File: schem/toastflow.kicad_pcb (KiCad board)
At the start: 2 copper layers, 40 x 25 mm, 23 parts, among them IC1 ATTINY13, K1 CONN_3, P1 CONN_3X2, SW1 SW_PUSH, U1 TRIAC

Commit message: Blank code
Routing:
- net VCC: track 54.1 -> 55.0 mm, vias 2 -> 1
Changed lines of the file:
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@@
     (links 38)
     (no_connects 0)
-    (area 0 0 0 0)
+    (area 32.924999 36.424999 75.486111 63.5196)
     (thickness 1.6)
     (drawings 8)
-    (tracks 107)
+    (tracks 102)
     (zones 0)
     (modules 23)
@@
       (viasonmask false)
       (mode 1)
-      (useauxorigin false)
+      (useauxorigin true)
       (hpglpennumber 1)
       (hpglpenspeed 20)
@@
     (fp_line (start 11.5 4.5) (end -11.5 4.5) (layer F.SilkS) (width 0.15))
     (fp_line (start -11.5 4.5) (end -11.5 -4.5) (layer F.SilkS) (width 0.15))
-    (pad 1 thru_hole circle (at -7.5 0) (size 1.8 1.8) (drill 1.2)
+    (pad 1 thru_hole circle (at -7.5 0) (size 1.8 1.8) (drill 1.199999)
       (layers *.Cu *.Mask F.SilkS)
       (net 8 N-0000013)
     )
-    (pad 2 thru_hole circle (at 7.5 0) (size 1.8 1.8) (drill 1.2)
+    (pad 2 thru_hole circle (at 7.5 0) (size 1.8 1.8) (drill 1.199999)
       (layers *.Cu *.Mask F.SilkS)
       (net 15 VCC)
@@
     (fp_line (start 5.25 3) (end -5.25 3) (layer F.SilkS) (width 0.15))
     (fp_line (start -5.25 3) (end -5.25 -4) (layer F.SilkS) (width 0.15))
-    (pad 1 thru_hole rect (at -3.5 0 270) (size 2 2) (drill 1.2)
+    (pad 1 thru_hole rect (at -3.5 0 270) (size 2 2) (drill 1.199999)
       (layers *.Cu *.Mask F.SilkS)
       (net 7 N-0000012)
     )
-    (pad 2 thru_hole circle (at 0 0 270) (size 2 2) (drill 1.2)
+    (pad 2 thru_hole circle (at 0 0 270) (size 2 2) (drill 1.199999)
       (layers *.Cu *.Mask F.SilkS)
       (net 13 N-000007)
     )
-    (pad 3 thru_hole circle (at 3.5 0 270) (size 2 2) (drill 1.2)
+    (pad 3 thru_hole circle (at 3.5 0 270) (size 2 2) (drill 1.199999)
       (layers *.Cu *.Mask F.SilkS)
       (net 8 N-0000013)
@@
     (fp_line (start 8.75 2.5) (end -8.75 2.5) (layer F.SilkS) (width 0.15))
     (fp_line (start -8.75 2.5) (end -8.75 -2.5) (layer F.SilkS) (width 0.15))
-    (pad 1 thru_hole circle (at -7.5 0) (size 1 1) (drill 0.6)
+    (pad 1 thru_hole circle (at -7.5 0) (size 1 1) (drill 0.599999)
       (layers *.Cu *.Mask F.SilkS)
       (net 13 N-000007)
     )
-    (pad 2 thru_hole circle (at 7.5 0) (size 1 1) (drill 0.6)
+    (pad 2 thru_hole circle (at 7.5 0) (size 1 1) (drill 0.599999)
       (layers *.Cu *.Mask F.SilkS)
       (net 12 N-000004)
@@
   (segment (start 52.962 41.238) (end 53.2 41.238) (width 0.3) (layer F.Cu) (net 14))
   (segment (start 51.1 43.1) (end 52.962 41.238) (width 0.3) (layer F.Cu) (net 14))
-  (segment (start 55.4 44.2) (end 55.000002 44.599998) (width 0.3) (layer B.Cu) (net 15))
-  (segment (start 58.15 42.75) (end 58.2 42.8) (width 0.3) (layer F.Cu) (net 15))
-  (via (at 58.2 42.8) (size 0.8) (layers F.Cu B.Cu) (net 15))
-  (segment (start 58.2 42.8) (end 56.8 42.8) (width 0.3) (layer B.Cu) (net 15))
-  (segment (start 56.8 42.8) (end 55.4 44.2) (width 0.3) (layer B.Cu) (net 15))
-  (segment (start 57 42.75) (end 58.15 42.75) (width 0.3) (layer F.Cu) (net 15))
-  (segment (start 55.000002 50.870002) (end 58.03 53.9) (width 0.3) (layer B.Cu) (net 15))
-  (segment (start 55.000002 50.300002) (end 55.000002 50.870002) (width 0.3) (layer B.Cu) (net 15))
-  (segment (start 55.000002 44.599998) (end 55.000002 50.300002) (width 0.3) (layer B.Cu) (net 15))
+  (segment (start 58.03 53.9) (end 55.000002 50.870002) (width 0.3) (layer B.Cu) (net 15) (status 400000))
+  (segment (start 57.7 41.8) (end 59.8 41.8) (width 0.3) (layer B.Cu) (net 15) (status 800000))
+  (segment (start 55.000002 44.499998) (end 57.7 41.8) (width 0.3) (layer B.Cu) (net 15))
+  (segment (start 55.000002 50.870002) (end 55.000002 44.499998) (width 0.3) (layer B.Cu) (net 15))
   (segment (start 58.03 53.9) (end 59.33 55.2) (width 0.3) (layer B.Cu) (net 15))
   (segment (start 59.33 55.2) (end 66.1 55.2) (width 0.3) (layer B.Cu) (net 15))

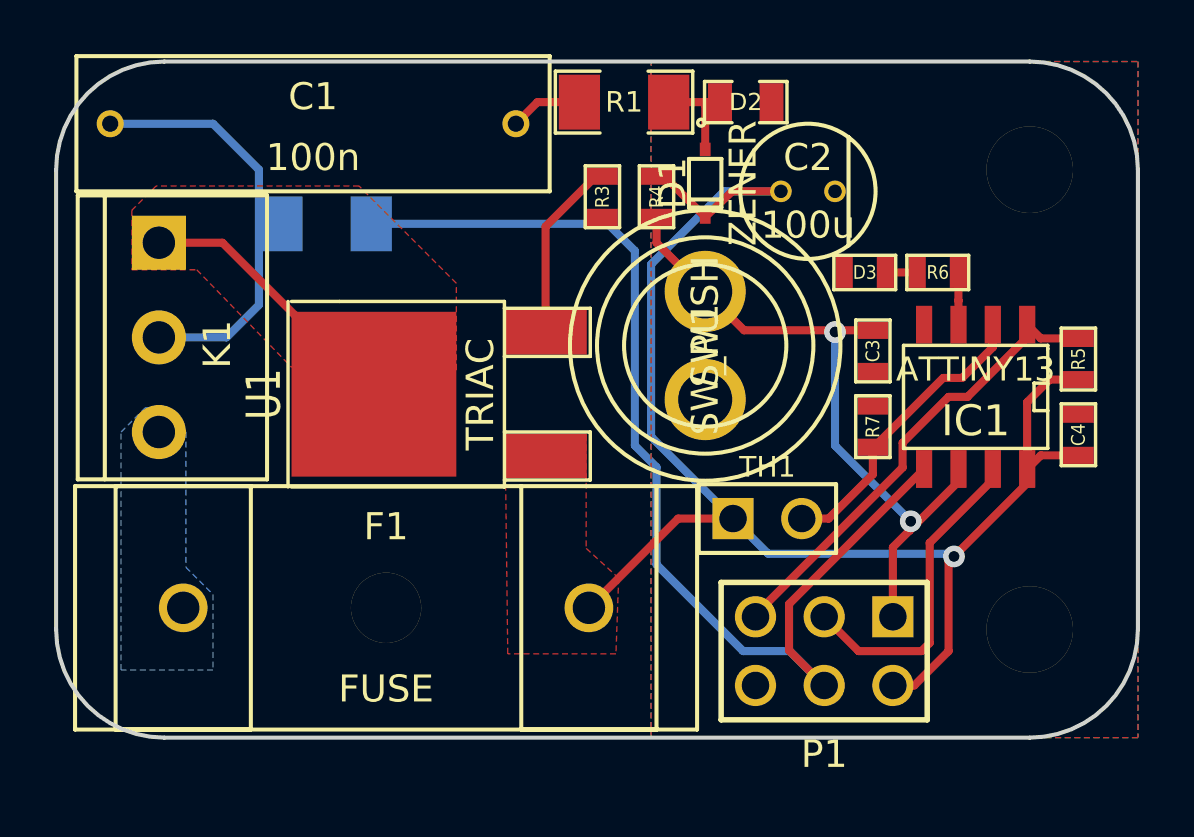
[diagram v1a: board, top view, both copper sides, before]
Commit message: Fixed triac pin.
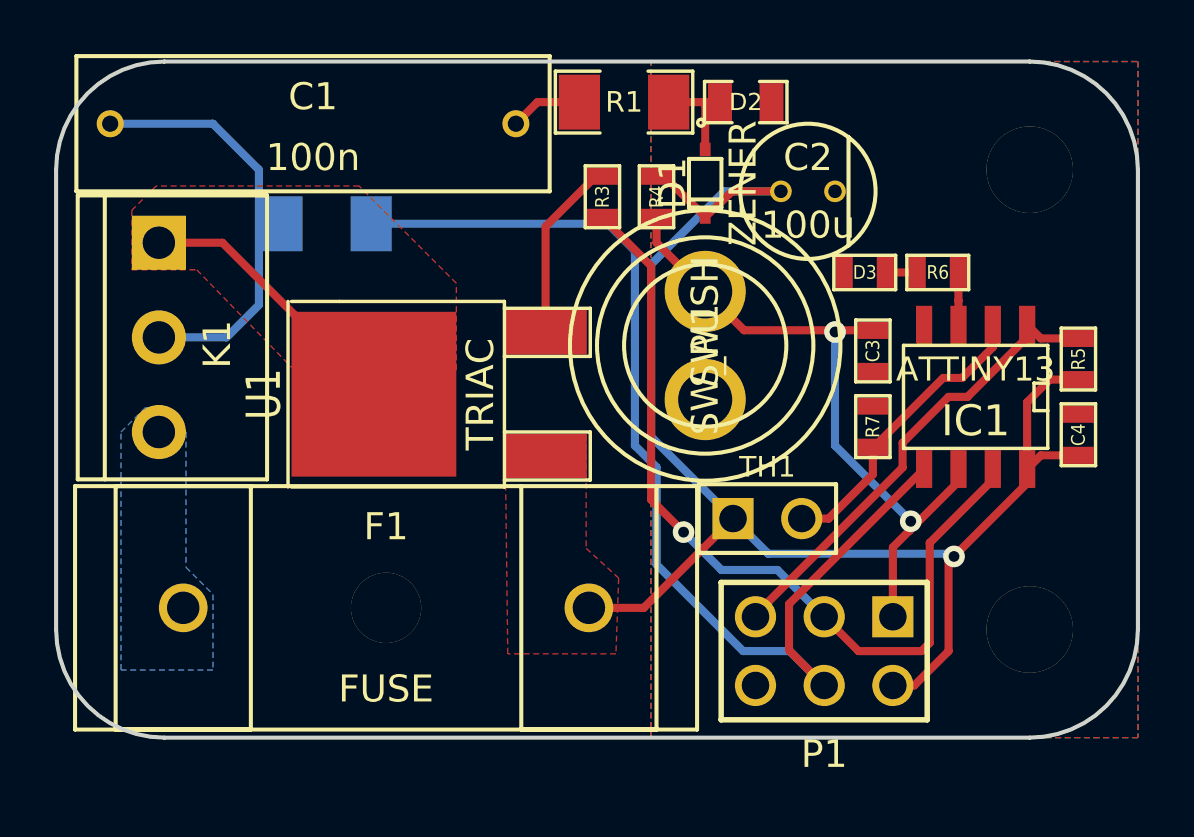
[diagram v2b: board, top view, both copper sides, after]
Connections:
- IC1 pad 7: N-0000010 -> /TRIAC
- P1 pad 3: N-0000010 -> /TRIAC
- R3 pad 2: (no net) -> /TRIAC
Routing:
- net /TRIAC: track 0.00 -> 31.3 mm, vias 0 -> 1
- net N-0000010: track 12.0 -> 0.00 mm
